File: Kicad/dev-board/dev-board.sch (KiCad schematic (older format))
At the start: 59 parts, among them J1 Conn_01x03_Male, J10 Conn_01x03_Male, J11 Conn_01x03_Male, J13 Conn_01x04_Male, J15 Conn_01x03_Male, J16 Conn_01x06_Male, J2 Conn_01x04_Male, J3 Conn_01x02_Male, J4 Conn_01x02_Male, J5 Conn_01x02_Male, J6 Conn_01x02_Male, J7 Conn_01x04_Male, J8 Conn_01x03_Male, J9 Conn_01x03_Male, Q1 2N2219, SW1 SW_DIP_x04, SW2 SW_SPDT, SW3 SW_SPDT, SW4 SW_Push, SW5 SW_Push, SW6 SW_Push, SW7 SW_Push, SW8 Rotary_Encoder_Switch, U1 NE555P

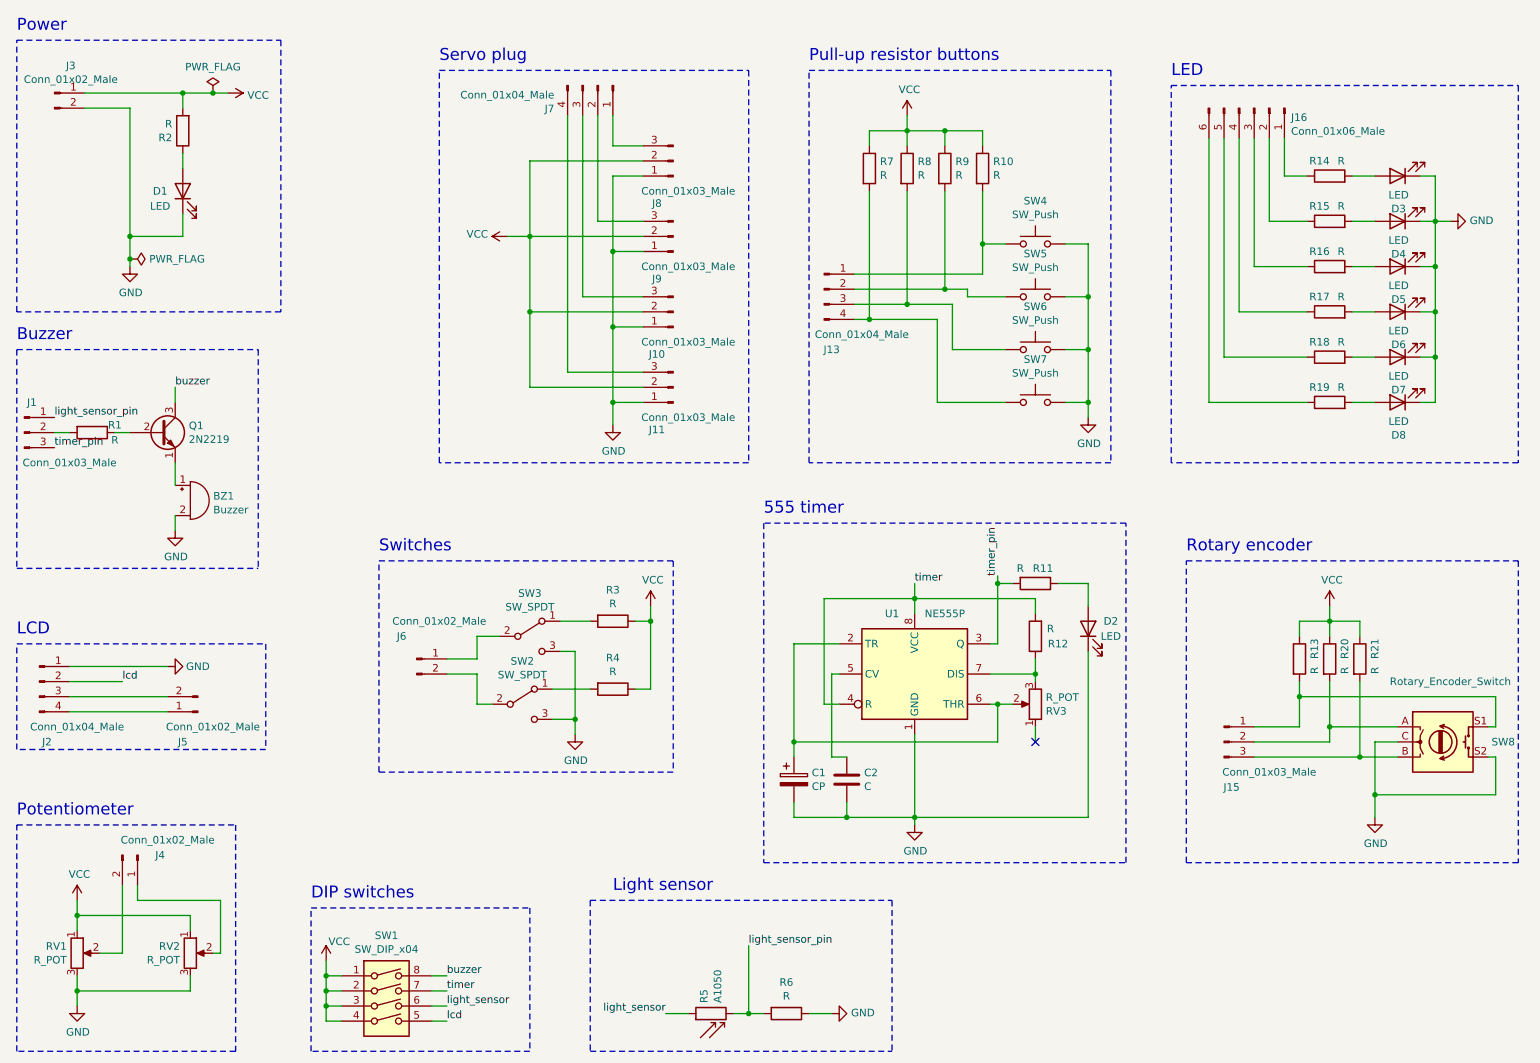
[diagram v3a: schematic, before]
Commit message: Add components values
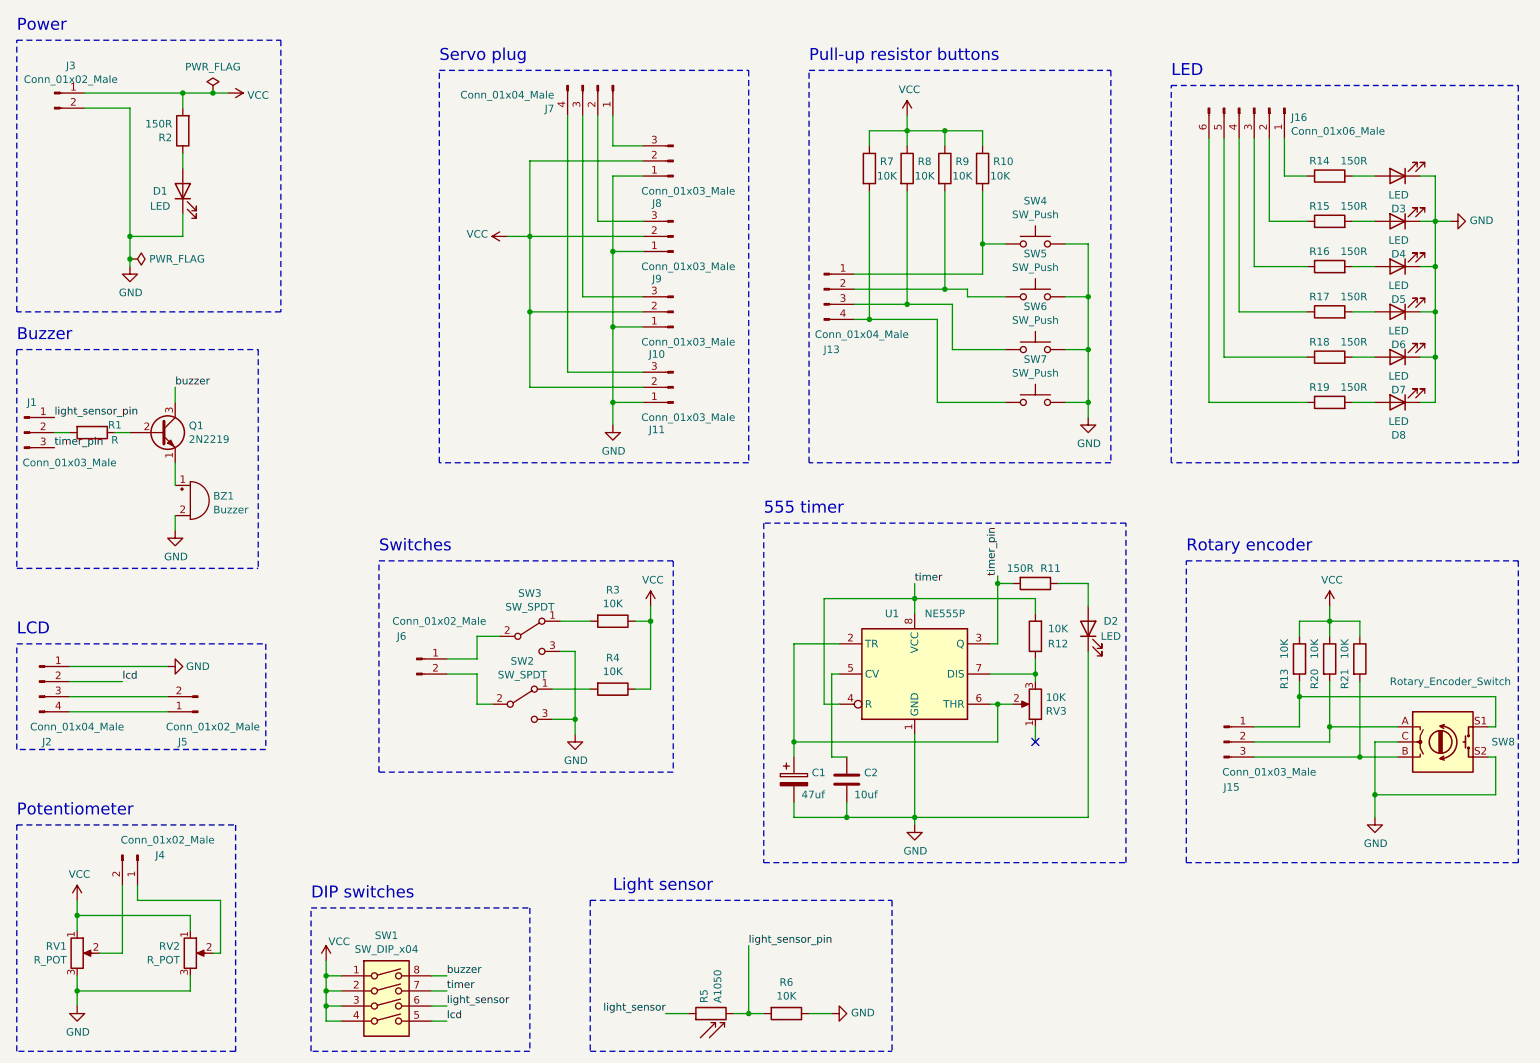
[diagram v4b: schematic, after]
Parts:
- C1: value CP -> 47uf
- C2: value C -> 10uf
- R10, R12, R13, R20, R21, R3, R4, R6, R7, R8, R9: value R -> 10K
- R11, R14, R15, R16, R17, R18, R19, R2: value R -> 150R
- RV3: value R_POT -> 10K
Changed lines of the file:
@@
 P 9550 2600
 F 0 "R17" V 9650 2600 50  0000 L CNN
-F 1 "R" V 9650 2500 50  0000 L CNN
+F 1 "150R" V 9650 2350 50  0000 L CNN
 F 2 "Resistor_SMD:R_0805_2012Metric_Pad1.15x1.40mm_HandSolder" V 9480 2600 50  0001 C CNN
 F 3 "~" H 9550 2600 50  0001 C CNN
@@
 P 9550 2900
 F 0 "R18" V 9650 2900 50  0000 L CNN
-F 1 "R" V 9650 2800 50  0000 L CNN
+F 1 "150R" V 9650 2650 50  0000 L CNN
 F 2 "Resistor_SMD:R_0805_2012Metric_Pad1.15x1.40mm_HandSolder" V 9480 2900 50  0001 C CNN
 F 3 "~" H 9550 2900 50  0001 C CNN
@@
 P 9550 3200
 F 0 "R19" V 9650 3200 50  0000 L CNN
-F 1 "R" V 9650 3100 50  0000 L CNN
+F 1 "150R" V 9650 2950 50  0000 L CNN
 F 2 "Resistor_SMD:R_0805_2012Metric_Pad1.15x1.40mm_HandSolder" V 9480 3200 50  0001 C CNN
 F 3 "~" H 9550 3200 50  0001 C CNN
@@
 P 9550 2000
 F 0 "R15" V 9650 2000 50  0000 L CNN
-F 1 "R" V 9650 1900 50  0000 L CNN
+F 1 "150R" V 9650 1750 50  0000 L CNN
 F 2 "Resistor_SMD:R_0805_2012Metric_Pad1.15x1.40mm_HandSolder" V 9480 2000 50  0001 C CNN
 F 3 "~" H 9550 2000 50  0001 C CNN
@@
 P 9550 2300
 F 0 "R16" V 9650 2300 50  0000 L CNN
-F 1 "R" V 9650 2200 50  0000 L CNN
+F 1 "150R" V 9650 2050 50  0000 L CNN
 F 2 "Resistor_SMD:R_0805_2012Metric_Pad1.15x1.40mm_HandSolder" V 9480 2300 50  0001 C CNN
 F 3 "~" H 9550 2300 50  0001 C CNN
@@
 P 1950 1400
 F 0 "R2" H 2020 1446 50  0000 L CNN
-F 1 "R" H 2020 1355 50  0000 L CNN
+F 1 "150R" H 2020 1355 50  0000 L CNN
 F 2 "Resistor_SMD:R_0805_2012Metric_Pad1.15x1.40mm_HandSolder" V 1880 1400 50  0001 C CNN
 F 3 "~" H 1950 1400 50  0001 C CNN
@@
 U 1 1 5F5800B5
 P 9550 4900
-F 0 "R20" V 9650 4900 50  0000 L CNN
-F 1 "R" V 9650 4800 50  0000 L CNN
+F 0 "R20" V 9450 4700 50  0000 L CNN
+F 1 "10K" V 9450 4900 50  0000 L CNN
 F 2 "Resistor_SMD:R_0805_2012Metric_Pad1.15x1.40mm_HandSolder" V 9480 4900 50  0001 C CNN
 F 3 "~" H 9550 4900 50  0001 C CNN
@@
 U 1 1 5F5804B3
 P 9350 4900
-F 0 "R13" V 9450 4900 50  0000 L CNN
-F 1 "R" V 9450 4800 50  0000 L CNN
+F 0 "R13" V 9250 4700 50  0000 L CNN
+F 1 "10K" V 9250 4900 50  0000 L CNN
 F 2 "Resistor_SMD:R_0805_2012Metric_Pad1.15x1.40mm_HandSolder" V 9280 4900 50  0001 C CNN
 F 3 "~" H 9350 4900 50  0001 C CNN
@@
 U 1 1 5F580702
 P 9750 4900
-F 0 "R21" V 9850 4900 50  0000 L CNN
-F 1 "R" V 9850 4800 50  0000 L CNN
+F 0 "R21" V 9650 4700 50  0000 L CNN
+F 1 "10K" V 9650 4900 50  0000 L CNN
 F 2 "Resistor_SMD:R_0805_2012Metric_Pad1.15x1.40mm_HandSolder" V 9680 4900 50  0001 C CNN
 F 3 "~" H 9750 4900 50  0001 C CNN
@@
 F 3 "" H 10350 2000 50  0001 C CNN
 	1    10350 2000
-	0    -1   -1   0
-$EndComp
-$Comp
-L Device:R R14
-U 1 1 5F573ABD
-P 9550 1700
-F 0 "R14" V 9650 1700 50  0000 L CNN
-F 1 "R" V 9650 1600 50  0000 L CNN
-F 2 "Resistor_SMD:R_0805_2012Metric_Pad1.15x1.40mm_HandSolder" V 9480 1700 50  0001 C CNN
-F 3 "~" H 9550 1700 50  0001 C CNN
-	1    9550 1700
 	0    -1   -1   0
 $EndComp
@@
 P 6500 1650
 F 0 "R7" H 6570 1696 50  0000 L CNN
-F 1 "R" H 6570 1605 50  0000 L CNN
+F 1 "10K" H 6550 1600 50  0000 L CNN
 F 2 "Resistor_SMD:R_0805_2012Metric_Pad1.15x1.40mm_HandSolder" V 6430 1650 50  0001 C CNN
 F 3 "~" H 6500 1650 50  0001 C CNN
@@
 P 6750 1650
 F 0 "R8" H 6820 1696 50  0000 L CNN
-F 1 "R" H 6820 1605 50  0000 L CNN
+F 1 "10K" H 6800 1600 50  0000 L CNN
 F 2 "Resistor_SMD:R_0805_2012Metric_Pad1.15x1.40mm_HandSolder" V 6680 1650 50  0001 C CNN
 F 3 "~" H 6750 1650 50  0001 C CNN
@@
 P 7000 1650
 F 0 "R9" H 7070 1696 50  0000 L CNN
-F 1 "R" H 7070 1605 50  0000 L CNN
+F 1 "10K" H 7050 1600 50  0000 L CNN
 F 2 "Resistor_SMD:R_0805_2012Metric_Pad1.15x1.40mm_HandSolder" V 6930 1650 50  0001 C CNN
 F 3 "~" H 7000 1650 50  0001 C CNN
@@
 P 7250 1650
 F 0 "R10" H 7320 1696 50  0000 L CNN
-F 1 "R" H 7320 1605 50  0000 L CNN
+F 1 "10K" H 7300 1600 50  0000 L CNN
 F 2 "Resistor_SMD:R_0805_2012Metric_Pad1.15x1.40mm_HandSolder" V 7180 1650 50  0001 C CNN
 F 3 "~" H 7250 1650 50  0001 C CNN
@@
 Wire Notes Line
 	850  7500 850  6000
-$Comp
-L Device:R R6
-U 1 1 5F7220ED
-P 5950 7250
-F 0 "R6" V 5743 7250 50  0000 C CNN
-F 1 "R" V 5834 7250 50  0000 C CNN
-F 2 "Resistor_SMD:R_0805_2012Metric_Pad1.15x1.40mm_HandSolder" V 5880 7250 50  0001 C CNN
-F 3 "~" H 5950 7250 50  0001 C CNN
-	1    5950 7250
-	0    1    1    0
-$EndComp
 Wire Wire Line
 	5300 7250 5150 7250
@@
 P 4800 4650
 F 0 "R3" V 4593 4650 50  0000 C CNN
-F 1 "R" V 4684 4650 50  0000 C CNN
+F 1 "10K" V 4684 4650 50  0000 C CNN
 F 2 "Resistor_SMD:R_0805_2012Metric_Pad1.15x1.40mm_HandSolder" V 4730 4650 50  0001 C CNN
 F 3 "~" H 4800 4650 50  0001 C CNN
@@
 P 4800 5100
 F 0 "R4" V 4593 5100 50  0000 C CNN
-F 1 "R" V 4684 5100 50  0000 C CNN
+F 1 "10K" V 4684 5100 50  0000 C CNN
 F 2 "Resistor_SMD:R_0805_2012Metric_Pad1.15x1.40mm_HandSolder" V 4730 5100 50  0001 C CNN
 F 3 "~" H 4800 5100 50  0001 C CNN
@@
 P 7600 4750
 F 0 "R12" H 7450 4800 50  0000 C CNN
-F 1 "R" H 7500 4700 50  0000 C CNN
+F 1 "10K" H 7450 4700 50  0000 C CNN
 F 2 "Resistor_SMD:R_0805_2012Metric_Pad1.15x1.40mm_HandSolder" V 7530 4750 50  0001 C CNN
 F 3 "~" H 7600 4750 50  0001 C CNN
@@
 P 7600 5200
 F 0 "RV3" H 7531 5246 50  0000 R CNN
-F 1 "R_POT" H 7531 5155 50  0000 R CNN
+F 1 "10K" H 7531 5155 50  0000 R CNN
 F 2 "Potentiometer_THT:Potentiometer_Piher_PT-6-V_Vertical" H 7600 5200 50  0001 C CNN
 F 3 "~" H 7600 5200 50  0001 C CNN
@@
 Wire Wire Line
 	6000 4800 6000 5450
-$Comp
-L Device:CP C1
-U 1 1 5F595DD0
-P 6000 5700
-F 0 "C1" H 6118 5746 50  0000 L CNN
-F 1 "CP" H 6118 5655 50  0000 L CNN
-F 2 "Capacitor_SMD:CP_Elec_5x5.3" H 6038 5550 50  0001 C CNN
-F 3 "~" H 6000 5700 50  0001 C CNN
-	1    6000 5700
-	1    0    0    -1
-$EndComp
 Wire Wire Line
 	6800 5400 6800 5950
@@
 U 1 1 5F8A38B9
 P 7600 4400
-F 0 "R11" V 7500 4450 50  0000 C CNN
-F 1 "R" V 7500 4300 50  0000 C CNN
+F 0 "R11" V 7500 4500 50  0000 C CNN
+F 1 "150R" V 7500 4300 50  0000 C CNN
 F 2 "Resistor_SMD:R_0805_2012Metric_Pad1.15x1.40mm_HandSolder" V 7530 4400 50  0001 C CNN
 F 3 "~" H 7600 4400 50  0001 C CNN
@@
 P 6350 5700
 F 0 "C2" H 6465 5746 50  0000 L CNN
-F 1 "C" H 6465 5655 50  0000 L CNN
+F 1 "10uf" H 6400 5600 50  0000 L CNN
 F 2 "Capacitor_SMD:C_0805_2012Metric_Pad1.15x1.40mm_HandSolder" H 6388 5550 50  0001 C CNN
 F 3 "~" H 6350 5700 50  0001 C CNN
@@
 Wire Wire Line
 	1100 3400 1200 3400
+$Comp
+L Device:R R14
+U 1 1 5F573ABD
+P 9550 1700
+F 0 "R14" V 9650 1700 50  0000 L CNN
+F 1 "150R" V 9650 1450 50  0000 L CNN
+F 2 "Resistor_SMD:R_0805_2012Metric_Pad1.15x1.40mm_HandSolder" V 9480 1700 50  0001 C CNN
+F 3 "~" H 9550 1700 50  0001 C CNN
+	1    9550 1700
+	0    -1   -1   0
+$EndComp
+$Comp
+L Device:CP C1
+U 1 1 5F595DD0
+P 6000 5700
+F 0 "C1" H 6118 5746 50  0000 L CNN
+F 1 "47uf" H 6050 5600 50  0000 L CNN
+F 2 "Capacitor_SMD:CP_Elec_5x5.3" H 6038 5550 50  0001 C CNN
+F 3 "~" H 6000 5700 50  0001 C CNN
+	1    6000 5700
+	1    0    0    -1
+$EndComp
+$Comp
+L Device:R R6
+U 1 1 5F7220ED
+P 5950 7250
+F 0 "R6" V 5743 7250 50  0000 C CNN
+F 1 "10K" V 5834 7250 50  0000 C CNN
+F 2 "Resistor_SMD:R_0805_2012Metric_Pad1.15x1.40mm_HandSolder" V 5880 7250 50  0001 C CNN
+F 3 "~" H 5950 7250 50  0001 C CNN
+	1    5950 7250
+	0    1    1    0
+$EndComp
 $EndSCHEMATC
